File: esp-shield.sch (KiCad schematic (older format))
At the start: 23 parts, among them J1 Conn_02x03_Counter_Clockwise, J2 Conn_01x08, J3 Conn_01x06, J4 Conn_01x08, SW1 RESET, SW2 PROG, U2 ESP-01

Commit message: Push unsaved things
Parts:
- U2: symbol ESP8266-01_ESP-01:ESP8266-01_ESP-01 -> esp-shield-rescue:ESP8266-01_ESP-01-ESP8266-01_ESP-01
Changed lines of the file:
@@
 RX_AR
 $Comp
-L ESP8266-01_ESP-01:ESP8266-01_ESP-01 U2
+L esp-shield-rescue:ESP8266-01_ESP-01-ESP8266-01_ESP-01 U2
 U 1 1 6198E5FA
 P 4750 5200

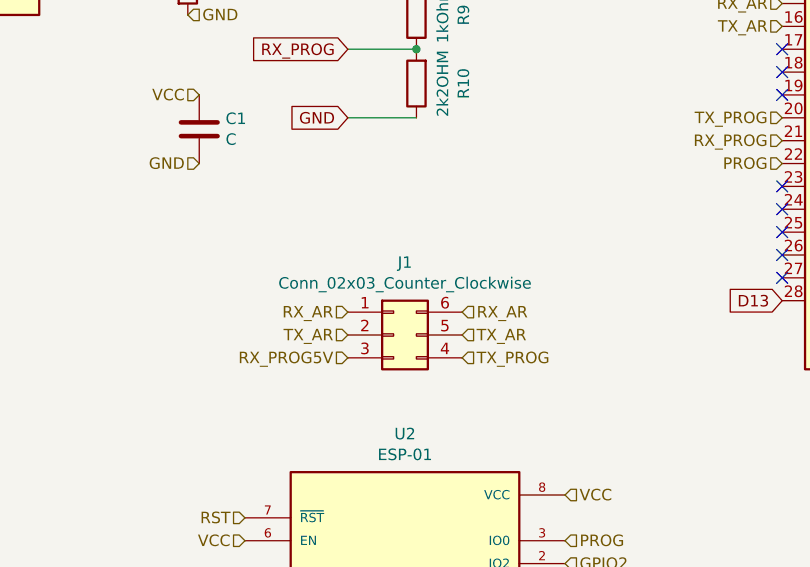
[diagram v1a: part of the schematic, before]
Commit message: Added Arduino pinout labels
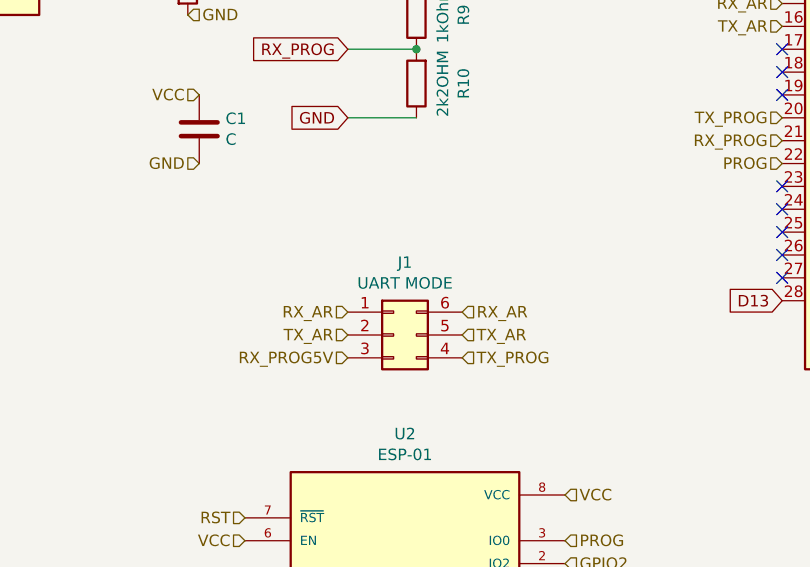
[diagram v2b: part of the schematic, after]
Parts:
- J1: value Conn_02x03_Counter_Clockwise -> UART MODE
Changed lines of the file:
@@
 P 4700 4200
 F 0 "J1" H 4750 4517 50  0000 C CNN
-F 1 "Conn_02x03_Counter_Clockwise" H 4750 4426 50  0000 C CNN
+F 1 "UART MODE" H 4750 4426 50  0000 C CNN
 F 2 "Connector_PinHeader_2.54mm:PinHeader_2x03_P2.54mm_Vertical" H 4700 4200 50  0001 C CNN
 F 3 "~" H 4700 4200 50  0001 C CNN
